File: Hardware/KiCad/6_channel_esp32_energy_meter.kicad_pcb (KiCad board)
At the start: 2 copper layers, 61 x 62.2 mm, 114 parts, among them IC1 ATM90E32AS, IC2 ATM90E32AS, IC3 LMR14020SDDA, J1 CONN_04, J16 PINHD-1X19, J2 CONN_04, J3 CONN_023.5MM, J4 9-12VAC, J5 PINHD1X1-SM1X01_SM, J6 PINHD1X1-SM1X01_SM, J8 PINHD1X1-SM1X01_SM, J9 PKS019-4011-0, U1 ESP32-DEVKITC-32D, Y1 16.384MHz, Y2 16.384MHz

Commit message: Make the schematic not terrible.
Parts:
- removed BR1: 50V/2A, 6_channel_esp32_energy_meter:SOP270P700X270-4
- removed C35: 10nF, 6_channel_esp32_energy_meter:C0603
- removed C36: 100uF/6.3V/1210, 6_channel_esp32_energy_meter:C1210
- removed CF1-2: BLU, 6_channel_esp32_energy_meter:CHIPLED_0603
- removed CT4-2, CT5-2, CT6-2: SJ2-35813B-SMT-TR, 6_channel_esp32_energy_meter:CUI_SJ2-35813B-SMT-TR
- removed D1: DIODE-DO214AC, 6_channel_esp32_energy_meter:DO214AC
- removed FD1, FD2: FIDUCIALUFIDUCIAL, 6_channel_esp32_energy_meter:FIDUCIAL-MICRO
- removed IC3: LMR14020SDDA, 6_channel_esp32_energy_meter:SOIC127P600X170-9N
- removed J16: PINHD-1X19, 6_channel_esp32_energy_meter:1X19
- removed J3: CONN_023.5MM, 6_channel_esp32_energy_meter:SCREWTERMINAL-3.5MM-2
- removed J4: 9-12VAC, 6_channel_esp32_energy_meter:CUI_PJ-002AH-SMT-TR
- removed J5, J6, J8: PINHD1X1-SM1X01_SM, 6_channel_esp32_energy_meter:1X01-SM
- removed J9: PKS019-4011-0, 6_channel_esp32_energy_meter:PKS01940110
- removed JP1, JP12, JP13, JP2, JP3, JP4, JP5, JP6: JUMPER-SMT_2_NC_TRACE_SILK, 6_channel_esp32_energy_meter:SMT-JUMPER_2_NC_TRACE_SILK
- removed L1: 3.3uH / 8x8mm, 6_channel_esp32_energy_meter:INDPM8082X300N
- removed LOGO1: OSHW-LOGOS, 6_channel_esp32_energy_meter:OSHW-LOGO-S
- removed PWR1: GRN, 6_channel_esp32_energy_meter:CHIPLED_0603
- removed U1: ESP32-DEVKITC-32D, 6_channel_esp32_energy_meter:MODULE_ESP32-DEVKITC-32D
- removed ZX0, ZX0-2, ZX1-2, ZX2-2: WIREPADSMD1,27-254, 6_channel_esp32_energy_meter:SMD1,27-2,54
- added CF2: BLU, 6_channel_esp32_energy_meter:CHIPLED_0603, F.Cu at (155.5, 113.0)
- added CF3: BLU, 6_channel_esp32_energy_meter:CHIPLED_0603, F.Cu at (153.8, 115.0)
- added CF4: BLU, 6_channel_esp32_energy_meter:CHIPLED_0603, F.Cu at (184.9, 83.3)
- added CF5: BLU, 6_channel_esp32_energy_meter:CHIPLED_0603, F.Cu at (186.6, 81.3)
- added CF6: BLU, 6_channel_esp32_energy_meter:CHIPLED_0603, F.Cu at (193.1, 75.2)
- added CF7: BLU, 6_channel_esp32_energy_meter:CHIPLED_0603, F.Cu at (122.6, 64.0)
- added CT1-1: SJ2-35813B-SMT-TR, 6_channel_esp32_energy_meter:CUI_SJ2-35813B-SMT-TR, F.Cu at (97.2, 74.9)
- added CT2-1: SJ2-35813B-SMT-TR, 6_channel_esp32_energy_meter:CUI_SJ2-35813B-SMT-TR, F.Cu at (97.2, 86.4)
- added CT3-1: SJ2-35813B-SMT-TR, 6_channel_esp32_energy_meter:CUI_SJ2-35813B-SMT-TR, F.Cu at (97.2, 97.8)
- added R25: 20K, Resistor_SMD:R_0603_1608Metric_Pad1.05x0.95mm_HandSolder, F.Cu at (168.9, 90.8)
- added R27: 20K, Resistor_SMD:R_0603_1608Metric_Pad1.05x0.95mm_HandSolder, F.Cu at (158.0, 86.5)
- added R29: 22, Resistor_SMD:R_0603_1608Metric_Pad1.05x0.95mm_HandSolder, F.Cu at (169.9, 87.0)
- added R30: 22, Resistor_SMD:R_0603_1608Metric_Pad1.05x0.95mm_HandSolder, F.Cu at (192.8, 73.1)
- added R31: 22, Resistor_SMD:R_0603_1608Metric_Pad1.05x0.95mm_HandSolder, F.Cu at (155.0, 88.5)
- added R33: 100, Resistor_SMD:R_0603_1608Metric_Pad1.05x0.95mm_HandSolder, F.Cu at (184.6, 81.1)
- added R35: 100, Resistor_SMD:R_0603_1608Metric_Pad1.05x0.95mm_HandSolder, F.Cu at (183.4, 71.1)
- added R36: 100, Resistor_SMD:R_0603_1608Metric_Pad1.05x0.95mm_HandSolder, F.Cu at (180.4, 73.1)
- added R37: 100, Resistor_SMD:R_0603_1608Metric_Pad1.05x0.95mm_HandSolder, F.Cu at (158.0, 88.5)
- added R38: 100, Resistor_SMD:R_0603_1608Metric_Pad1.05x0.95mm_HandSolder, F.Cu at (165.9, 85.0)
- added R39: 1K, Resistor_SMD:R_0603_1608Metric_Pad1.05x0.95mm_HandSolder, F.Cu at (175.7, 82.4)
- added R40: 1K, Resistor_SMD:R_0603_1608Metric_Pad1.05x0.95mm_HandSolder, F.Cu at (186.9, 79.1)
- added R41: 10K, Resistor_SMD:R_0603_1608Metric_Pad1.05x0.95mm_HandSolder, F.Cu at (180.4, 71.1)
- added R42: 220, Resistor_SMD:R_0603_1608Metric_Pad1.05x0.95mm_HandSolder, F.Cu at (172.9, 87.0)
- added R43: 10K, Resistor_SMD:R_0603_1608Metric_Pad1.05x0.95mm_HandSolder, F.Cu at (163.9, 87.0)
- added R44: 1k, Resistor_SMD:R_0603_1608Metric_Pad1.05x0.95mm_HandSolder, F.Cu at (168.9, 85.0)
- added R45: 1k, Resistor_SMD:R_0603_1608Metric_Pad1.05x0.95mm_HandSolder, F.Cu at (183.9, 75.1)
- added R46: 1k, Resistor_SMD:R_0603_1608Metric_Pad1.05x0.95mm_HandSolder, F.Cu at (183.9, 73.1)
- added R47: 1k, 6_channel_esp32_energy_meter:R0603, F.Cu at (131.6, 69.1)
- added ZX10: WIREPADSMD1,27-254, 6_channel_esp32_energy_meter:SMD1,27-2,54, F.Cu at (189.0, 77.4)
- added ZX11: WIREPADSMD1,27-254, 6_channel_esp32_energy_meter:SMD1,27-2,54, F.Cu at (192.0, 75.4)
- added ZX12: WIREPADSMD1,27-254, 6_channel_esp32_energy_meter:SMD1,27-2,54, F.Cu at (183.8, 83.4)
- added ZX13: WIREPADSMD1,27-254, 6_channel_esp32_energy_meter:SMD1,27-2,54, F.Cu at (181.0, 86.7)
- added ZX14: WIREPADSMD1,27-254, 6_channel_esp32_energy_meter:SMD1,27-2,54, F.Cu at (190.3, 77.4)
- added ZX3: WIREPADSMD1,27-254, 6_channel_esp32_energy_meter:SMD1,27-2,54, F.Cu at (149.9, 118.4)
- added ZX4: WIREPADSMD1,27-254, 6_channel_esp32_energy_meter:SMD1,27-2,54, F.Cu at (137.6, 108.3)
- added ZX5: WIREPADSMD1,27-254, 6_channel_esp32_energy_meter:SMD1,27-2,54, F.Cu at (143.3, 95.1)
- added ZX6: WIREPADSMD1,27-254, 6_channel_esp32_energy_meter:SMD1,27-2,54, F.Cu at (136.3, 108.3)
- added ZX7: WIREPADSMD1,27-254, 6_channel_esp32_energy_meter:SMD1,27-2,54, F.Cu at (143.3, 97.6)
- added ZX8: WIREPADSMD1,27-254, 6_channel_esp32_energy_meter:SMD1,27-2,54, F.Cu at (195.9, 64.1)
- added ZX9: WIREPADSMD1,27-254, 6_channel_esp32_energy_meter:SMD1,27-2,54, F.Cu at (195.9, 66.7)
- C1, C10, C26, C9: value 0.1uF -> 18nF
- C14, C29: value 18nF -> 10uF
- C15, C30: value 18nF -> 0.1uF
- C17: value .33uF -> 0.1uF
- C18, C22, C5: value .33uF -> 18nF
- C23, C8: value 10uF -> .33uF
- C24, C25: value 0.1uF -> .33uF
- C27: value 10uF -> 18nF
- C31: value 0.1uF -> 10uF
- C32: value 220pF -> 0.1uF
- C33: value 100uF/25V -> 0.1uF; footprint 6_channel_esp32_energy_meter:UD-6,3X7,7_NICHICON -> 6_channel_esp32_energy_meter:C0603
- C34: value 10uF/25V -> 0.1uF; footprint 6_channel_esp32_energy_meter:C0805 -> 6_channel_esp32_energy_meter:C0603
- IC1, IC2: value ATM90E32AS -> ATM90E36
- J1: value CONN_04 -> Conn_02x05_Odd_Even; footprint 6_channel_esp32_energy_meter:1X04 -> Connector_IDC:IDC-Header_2x05_P2.54mm_Vertical
- J2: value CONN_04 -> Conn_02x07_Odd_Even; footprint 6_channel_esp32_energy_meter:1X04 -> Connector_IDC:IDC-Header_2x07_P2.54mm_Vertical
- R1: value 10K -> 20K; footprint 6_channel_esp32_energy_meter:R0603 -> Resistor_SMD:R_0603_1608Metric_Pad1.05x0.95mm_HandSolder
- R10: value 1k -> 100; footprint 6_channel_esp32_energy_meter:R0603 -> Resistor_SMD:R_0603_1608Metric_Pad1.05x0.95mm_HandSolder
- R11: value 1K -> 100; footprint 6_channel_esp32_energy_meter:RA1206-8 -> Resistor_SMD:R_0603_1608Metric_Pad1.05x0.95mm_HandSolder
- R12: value 10K -> 100; footprint 6_channel_esp32_energy_meter:R0603 -> Resistor_SMD:R_0603_1608Metric_Pad1.05x0.95mm_HandSolder
- R13: value 10K -> 100; footprint 6_channel_esp32_energy_meter:RA1206-8 -> Resistor_SMD:R_0603_1608Metric_Pad1.05x0.95mm_HandSolder
- R14, R24: footprint 6_channel_esp32_energy_meter:RA1206-8 -> Resistor_SMD:R_0603_1608Metric_Pad1.05x0.95mm_HandSolder
- R15, R6, R7, R8: footprint 6_channel_esp32_energy_meter:R0603 -> Resistor_SMD:R_0603_1608Metric_Pad1.05x0.95mm_HandSolder
- R16, R5: value 100 -> 1K; footprint 6_channel_esp32_energy_meter:R0603 -> Resistor_SMD:R_0603_1608Metric_Pad1.05x0.95mm_HandSolder
- R17: value 22 -> 1K; footprint 6_channel_esp32_energy_meter:R0603 -> Resistor_SMD:R_0603_1608Metric_Pad1.05x0.95mm_HandSolder
- R18: value 22 -> 10K; footprint 6_channel_esp32_energy_meter:R0603 -> Resistor_SMD:R_0603_1608Metric_Pad1.05x0.95mm_HandSolder
- R19: value 22 -> 220; footprint 6_channel_esp32_energy_meter:R0603 -> Resistor_SMD:R_0603_1608Metric_Pad1.05x0.95mm_HandSolder
- R2: value 10K -> 20K; footprint 6_channel_esp32_energy_meter:RA1206-8 -> Resistor_SMD:R_0603_1608Metric_Pad1.05x0.95mm_HandSolder
- R20: value 1k -> 10K; footprint 6_channel_esp32_energy_meter:R0603 -> Resistor_SMD:R_0603_1608Metric_Pad1.05x0.95mm_HandSolder
- R21: value 20k -> 1k; footprint 6_channel_esp32_energy_meter:R0603 -> Resistor_SMD:R_0603_1608Metric_Pad1.05x0.95mm_HandSolder
- R22: value 34k -> 1k; footprint 6_channel_esp32_energy_meter:R0603 -> Resistor_SMD:R_0603_1608Metric_Pad1.05x0.95mm_HandSolder
- R23: value 10k -> 1k; footprint 6_channel_esp32_energy_meter:R0603 -> Resistor_SMD:R_0603_1608Metric_Pad1.05x0.95mm_HandSolder
- R26: value 20k 1/4W -> 20K; footprint 6_channel_esp32_energy_meter:R0603 -> Resistor_SMD:R_0603_1608Metric_Pad1.05x0.95mm_HandSolder
- R28, R32: value 20k 1/4W -> 1K; footprint 6_channel_esp32_energy_meter:R0603 -> Resistor_SMD:R_0603_1608Metric_Pad1.05x0.95mm_HandSolder
- R3: value 100 -> 20K; footprint 6_channel_esp32_energy_meter:RA1206-8 -> Resistor_SMD:R_0603_1608Metric_Pad1.05x0.95mm_HandSolder
- R34: value 20k 1/4W -> 100; footprint 6_channel_esp32_energy_meter:R0603 -> Resistor_SMD:R_0603_1608Metric_Pad1.05x0.95mm_HandSolder
- R4: value 100 -> 20K; footprint 6_channel_esp32_energy_meter:R0603 -> Resistor_SMD:R_0603_1608Metric_Pad1.05x0.95mm_HandSolder
- R9: value 1k -> 1K; footprint 6_channel_esp32_energy_meter:R0603 -> Resistor_SMD:R_0603_1608Metric_Pad1.05x0.95mm_HandSolder
- ZX1, ZX2: moved to F.Cu
- moved CT4 100.1 mm to (107.3, 39.4), turned to 270 degrees
- moved CT5 82.9 mm to (107.3, 50.8), turned to 270 degrees
- moved CT6 70.8 mm to (107.3, 62.2), turned to 270 degrees
- moved J1 68.1 mm to (188.6, 102.2), turned to 0 degrees
- moved C34 62.6 mm to (180.8, 84.4), turned to 0 degrees
- moved C31 61.7 mm to (186.9, 77.1), turned to 0 degrees
- moved C32 57.9 mm to (189.9, 75.1), turned to 0 degrees
- moved C26 55.9 mm to (192.4, 71.1), turned to 0 degrees
- moved CT3-2 55.7 mm to (97.2, 63.5)
- moved CT2-2 53.5 mm to (97.2, 52.1)
- moved CT1-2 51.3 mm to (97.2, 40.6)
- moved C23 50.3 mm to (186.9, 75.1), turned to 0 degrees
- moved C33 48.7 mm to (178.9, 86.4), turned to 0 degrees
- moved R32 48.4 mm to (189.4, 71.1), turned to 0 degrees
- moved R10 48.0 mm to (131.2, 108.0), turned to 0 degrees
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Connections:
- C1 pad 1: GND -> (no net)
- C1 pad 2: Net-(C1-Pad2) -> (no net)
- C10 pad 1: GND -> (no net)
- C10 pad 2: VDD -> (no net)
- C11 pad 1: GND -> (no net)
- C11 pad 2: VDD -> (no net)
- C12 pad 1: Net-(C12-Pad1) -> (no net)
- C12 pad 2: GND -> (no net)
- C13 pad 1: Net-(C12-Pad1) -> (no net)
- C13 pad 2: GND -> (no net)
- C14 pad 1: VAP -> (no net)
- C14 pad 2: GND -> (no net)
- C15 pad 1: VAN -> (no net)
- C15 pad 2: GND -> (no net)
- C16 pad 1: GND -> (no net)
- C16 pad 2: Net-(C16-Pad2) -> (no net)
- C17 pad 1: /6_channel_esp32_energy_meter_2/IAP-2 -> (no net)
- C17 pad 2: GND -> (no net)
- C18 pad 1: GND -> (no net)
- C18 pad 2: /6_channel_esp32_energy_meter_2/IAN-2 -> (no net)
- C19 pad 1: /6_channel_esp32_energy_meter_2/IBP-2 -> (no net)
- C19 pad 2: GND -> (no net)
- C2 pad 1: /6_channel_esp32_energy_meter_1/IAP -> (no net)
- C2 pad 2: GND -> (no net)
- C20 pad 1: GND -> (no net)
- C20 pad 2: /6_channel_esp32_energy_meter_2/IBN-2 -> (no net)
- C21 pad 1: /6_channel_esp32_energy_meter_2/ICP-2 -> (no net)
- C21 pad 2: GND -> (no net)
- C22 pad 1: GND -> (no net)
- C22 pad 2: /6_channel_esp32_energy_meter_2/ICN-2 -> (no net)
- C23 pad 1: GND -> (no net)
- C23 pad 2: Net-(C23-Pad2) -> (no net)
- C24 pad 1: GND -> (no net)
- C24 pad 2: Net-(C23-Pad2) -> (no net)
- C25 pad 1: GND -> (no net)
- C25 pad 2: VDD -> (no net)
- C26 pad 1: GND -> (no net)
- C26 pad 2: VDD -> (no net)
- C27 pad 1: Net-(C27-Pad1) -> (no net)
- C27 pad 2: GND -> (no net)
- C28 pad 1: Net-(C27-Pad1) -> (no net)
- C28 pad 2: GND -> (no net)
- C29 pad 1: VAP2 -> (no net)
- C29 pad 2: GND -> (no net)
- C3 pad 1: GND -> (no net)
- C3 pad 2: /6_channel_esp32_energy_meter_1/IAN -> (no net)
- C30 pad 1: VAN2 -> (no net)
- C30 pad 2: GND -> (no net)
- C31 pad 1: Net-(C31-Pad1) -> (no net)
- C31 pad 2: Net-(C31-Pad2) -> (no net)
- C32 pad 1: VDD -> (no net)
- C32 pad 2: Net-(C32-Pad2) -> (no net)
- C34 pad 1: Net-(BR1-Pad1) -> (no net)
- C34 pad 2: GND -> (no net)
- C4 pad 1: /6_channel_esp32_energy_meter_1/IBP -> (no net)
- C4 pad 2: GND -> (no net)
- C5 pad 1: GND -> (no net)
- C5 pad 2: /6_channel_esp32_energy_meter_1/IBN -> (no net)
- C6 pad 1: /6_channel_esp32_energy_meter_1/ICP -> (no net)
- C6 pad 2: GND -> (no net)
- C7 pad 1: GND -> (no net)
- C7 pad 2: /6_channel_esp32_energy_meter_1/ICN -> (no net)
- C8 pad 1: GND -> (no net)
- C8 pad 2: Net-(C8-Pad2) -> (no net)
- C9 pad 1: GND -> (no net)
- C9 pad 2: Net-(C8-Pad2) -> (no net)
- CT1 pad 1: IA- -> Net-(CT1-1-Pad1)
- CT1 pad 2: IA+ -> Net-(CT1-1-Pad2)
- CT1-2 pad 1: IA- -> Net-(CT1-2-Pad1)
- CT1-2 pad 2: IA+ -> Net-(CT1-2-Pad2)
- CT2 pad 1: IB- -> Net-(CT2-1-Pad1)
- CT2 pad 2: IB+ -> Net-(CT2-1-Pad2)
- CT2-2 pad 1: IB- -> Net-(CT2-2-Pad1)
- CT2-2 pad 2: IB+ -> Net-(CT2-2-Pad2)
- CT3 pad 1: IC- -> Net-(CT3-1-Pad1)
- CT3 pad 2: IC+ -> Net-(CT3-1-Pad2)
- CT3-2 pad 1: IC- -> Net-(CT3-2-Pad1)
- CT3-2 pad 2: IC+ -> Net-(CT3-2-Pad2)
- CT4 pad 1: IA--2 -> Net-(CT1-2-Pad1)
- CT4 pad 2: IA+-2 -> Net-(CT1-2-Pad2)
- CT5 pad 1: IB--2 -> Net-(CT2-2-Pad1)
- CT5 pad 2: IB+-2 -> Net-(CT2-2-Pad2)
- CT6 pad 1: IC--2 -> Net-(CT3-2-Pad1)
- CT6 pad 2: IC+-2 -> Net-(CT3-2-Pad2)
- IC1 pad 1: VDD -> +3V3
- IC1 pad 10: Net-(IC1-Pad10) -> GND
- IC1 pad 11: Net-(C12-Pad1) -> Net-(IC1-Pad11)
- IC1 pad 13: VAP -> Net-(IC1-Pad13)
- IC1 pad 14: VAN -> Net-(IC1-Pad14)
- IC1 pad 15: VAP -> Net-(IC1-Pad15)
- IC1 pad 16: VAN -> Net-(IC1-Pad16)
- IC1 pad 17: VAP -> Net-(IC1-Pad17)
- IC1 pad 18: VAN -> Net-(IC1-Pad18)
- IC1 pad 22: /6_channel_esp32_energy_meter_1/ZX0 -> Net-(IC1-Pad22)
- IC1 pad 23: /6_channel_esp32_energy_meter_1/ZX1 -> Net-(IC1-Pad23)
- IC1 pad 24: /6_channel_esp32_energy_meter_1/ZX2 -> Net-(IC1-Pad24)
- IC1 pad 25: /6_channel_esp32_energy_meter_1/CF1 -> Net-(IC1-Pad25)
- IC1 pad 26: /6_channel_esp32_energy_meter_1/CF2 -> Net-(IC1-Pad26)
- IC1 pad 27: /6_channel_esp32_energy_meter_1/CF3 -> Net-(IC1-Pad27)
- IC1 pad 28: /6_channel_esp32_energy_meter_1/CF4 -> Net-(IC1-Pad28)
- IC1 pad 29: WARN -> Net-(IC1-Pad29)
- IC1 pad 3: /6_channel_esp32_energy_meter_1/IAP -> Net-(IC1-Pad3)
- IC1 pad 30: IRQ0 -> Net-(IC1-Pad30)
- IC1 pad 31: IRQ1 -> /meter_1/IRQ1
- IC1 pad 33: VDD -> +3V3
- IC1 pad 34: VDD -> +3V3
- IC1 pad 37: ~CS -> /meter_1/~CS
- IC1 pad 38: SCLK -> /meter_1/SCLK
- IC1 pad 39: MISO -> Net-(IC1-Pad39)
- IC1 pad 4: /6_channel_esp32_energy_meter_1/IAN -> Net-(IC1-Pad4)
- IC1 pad 40: MOSI -> /meter_1/SDI
- IC1 pad 41: Net-(C1-Pad2) -> /meter_1/~RESET
- IC1 pad 42: Net-(C8-Pad2) -> +3V3
- IC1 pad 43: Net-(C8-Pad2) -> +3V3
- IC1 pad 48: VDD -> +3V3
- IC1 pad 5: /6_channel_esp32_energy_meter_1/IBP -> Net-(IC1-Pad5)
- IC1 pad 6: /6_channel_esp32_energy_meter_1/IBN -> Net-(IC1-Pad6)
- IC1 pad 7: /6_channel_esp32_energy_meter_1/ICP -> Net-(IC1-Pad7)
- IC1 pad 8: /6_channel_esp32_energy_meter_1/ICN -> Net-(IC1-Pad8)
- IC1 pad 9: Net-(IC1-Pad9) -> GND
- IC2 pad 1: VDD -> +3V3
- IC2 pad 10: Net-(IC2-Pad10) -> GND
- IC2 pad 11: Net-(C27-Pad1) -> Net-(IC2-Pad11)
- IC2 pad 13: VAP2 -> Net-(IC2-Pad13)
- IC2 pad 14: VAN2 -> Net-(IC2-Pad14)
- IC2 pad 15: VAP2 -> Net-(IC2-Pad15)
- IC2 pad 16: VAN2 -> Net-(IC2-Pad16)
- IC2 pad 17: VAP2 -> Net-(IC2-Pad17)
- IC2 pad 18: VAN2 -> Net-(IC2-Pad18)
- IC2 pad 22: /6_channel_esp32_energy_meter_2/ZX0-2 -> Net-(IC2-Pad22)
- IC2 pad 23: /6_channel_esp32_energy_meter_2/ZX1-2 -> Net-(IC2-Pad23)
- IC2 pad 24: /6_channel_esp32_energy_meter_2/ZX2-2 -> Net-(IC2-Pad24)
- IC2 pad 25: /6_channel_esp32_energy_meter_2/CF1-2 -> Net-(IC2-Pad25)
- IC2 pad 26: /6_channel_esp32_energy_meter_2/CF2-2 -> Net-(IC2-Pad26)
- IC2 pad 27: /6_channel_esp32_energy_meter_2/CF3-2 -> Net-(IC2-Pad27)
- IC2 pad 28: /6_channel_esp32_energy_meter_2/CF4-2 -> Net-(IC2-Pad28)
- IC2 pad 29: WARN -> Net-(IC2-Pad29)
- IC2 pad 3: /6_channel_esp32_energy_meter_2/IAP-2 -> Net-(IC2-Pad3)
- IC2 pad 30: IRQ0 -> Net-(IC2-Pad30)
- IC2 pad 31: IRQ1 -> /meter_2/IRQ1
- IC2 pad 33: VDD -> +3V3
- IC2 pad 34: VDD -> +3V3
- IC2 pad 37: ~CS-2 -> /meter_2/~CS
- IC2 pad 38: SCLK -> /meter_1/SCLK
- IC2 pad 39: MISO -> Net-(IC2-Pad39)
- IC2 pad 4: /6_channel_esp32_energy_meter_2/IAN-2 -> Net-(IC2-Pad4)
- IC2 pad 40: MOSI -> /meter_1/SDI
- IC2 pad 41: Net-(C16-Pad2) -> /meter_1/~RESET
- IC2 pad 42: Net-(C23-Pad2) -> +3V3
- IC2 pad 43: Net-(C23-Pad2) -> +3V3
- IC2 pad 48: VDD -> +3V3
- IC2 pad 5: /6_channel_esp32_energy_meter_2/IBP-2 -> Net-(IC2-Pad5)
- IC2 pad 6: /6_channel_esp32_energy_meter_2/IBN-2 -> Net-(IC2-Pad6)
- IC2 pad 7: /6_channel_esp32_energy_meter_2/ICP-2 -> Net-(IC2-Pad7)
- IC2 pad 8: /6_channel_esp32_energy_meter_2/ICN-2 -> Net-(IC2-Pad8)
- IC2 pad 9: Net-(IC2-Pad9) -> GND
- J1 pad 1: /6_channel_esp32_energy_meter_1/CF4 -> /meter_1/V1P
- J1 pad 2: /6_channel_esp32_energy_meter_1/CF3 -> /meter_1/V1N
- J1 pad 3: /6_channel_esp32_energy_meter_1/CF2 -> /meter_1/V1P
- J1 pad 4: /6_channel_esp32_energy_meter_1/CF1 -> /meter_1/V1N
- J2 pad 1: /6_channel_esp32_energy_meter_2/CF4-2 -> +3V3
- J2 pad 2: /6_channel_esp32_energy_meter_2/CF3-2 -> +3V3
- J2 pad 3: /6_channel_esp32_energy_meter_2/CF2-2 -> /meter_1/~CS
- J2 pad 4: /6_channel_esp32_energy_meter_2/CF1-2 -> /meter_2/~CS
- R1 pad 1: VDD -> (no net)
- R1 pad 2: Net-(C1-Pad2) -> (no net)
- R10 pad 1: Net-(PWR1-PadA) -> (no net)
- R10 pad 2: VDD -> (no net)
- R11 pad 1: GND -> (no net)
- R11 pad 2: GND -> (no net)
- R12 pad 1: VDD -> (no net)
- R12 pad 2: Net-(C16-Pad2) -> (no net)
- R13 pad 1: MOSI -> (no net)
- R13 pad 2: MISO -> (no net)
- R14 pad 1: IA+-2 -> (no net)
- R14 pad 2: IA--2 -> (no net)
- R15 pad 1: /6_channel_esp32_energy_meter_2/ICP-2 -> (no net)
- R15 pad 2: IC+-2 -> (no net)
- R16 pad 1: /6_channel_esp32_energy_meter_2/ICN-2 -> (no net)
- R16 pad 2: IC--2 -> (no net)
- R17 pad 1: Net-(JP6-Pad1) -> (no net)
- R17 pad 2: IC+-2 -> (no net)
- R18 pad 1: Net-(JP4-Pad1) -> (no net)
- R18 pad 2: IA+-2 -> (no net)
- R19 pad 1: Net-(JP5-Pad1) -> (no net)
- R19 pad 2: IB+-2 -> (no net)
- R2 pad 1: MOSI -> (no net)
- R2 pad 2: MISO -> (no net)
- R20 pad 1: Net-(CF1-2-PadA) -> (no net)
- R20 pad 2: /6_channel_esp32_energy_meter_2/CF1-2 -> (no net)
- R21 pad 1: GND -> (no net)
- R21 pad 2: Net-(IC3-Pad4) -> (no net)
- R22 pad 1: Net-(C32-Pad2) -> (no net)
- R22 pad 2: VDD -> (no net)
- R23 pad 1: GND -> (no net)
- R23 pad 2: Net-(C32-Pad2) -> (no net)
- R24 pad 1: VDD -> (no net)
- R24 pad 2: VDD -> (no net)
- R26 pad 1: VAP -> (no net)
- R26 pad 2: /6_channel_esp32_energy_meter_3/VA+ -> (no net)
- R28 pad 1: VAP2 -> (no net)
- R28 pad 2: /6_channel_esp32_energy_meter_3/VA2+ -> (no net)
- R3 pad 1: IA+ -> (no net)
- R3 pad 2: IA- -> (no net)
- R32 pad 1: VAN2 -> (no net)
- R32 pad 2: /6_channel_esp32_energy_meter_3/VA2- -> (no net)
- R34 pad 1: VAN -> (no net)
- R34 pad 2: /6_channel_esp32_energy_meter_3/VA- -> (no net)
- R4 pad 1: /6_channel_esp32_energy_meter_1/ICP -> (no net)
- R4 pad 2: IC+ -> (no net)
- R5 pad 1: /6_channel_esp32_energy_meter_1/ICN -> (no net)
- R5 pad 2: IC- -> (no net)
- R6 pad 1: Net-(JP3-Pad1) -> (no net)
- R6 pad 2: IC+ -> (no net)
- R7 pad 1: Net-(JP1-Pad1) -> (no net)
- R7 pad 2: IA+ -> (no net)
- R8 pad 1: Net-(JP2-Pad1) -> (no net)
- R8 pad 2: IB+ -> (no net)
- R9 pad 1: Net-(CF1-PadA) -> (no net)
- R9 pad 2: /6_channel_esp32_energy_meter_1/CF1 -> (no net)
- ZX1 pad 1: /6_channel_esp32_energy_meter_1/ZX1 -> Net-(IC1-Pad22)
- ZX2 pad 1: /6_channel_esp32_energy_meter_1/ZX2 -> Net-(IC1-Pad23)
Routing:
- net VDD: track 276.3 -> 0.00 mm, vias 10 -> 0
- net IC+: track 137.4 -> 0.00 mm, vias 3 -> 0
- net IC-: track 113.8 -> 0.00 mm, vias 1 -> 0
- net IB+: track 99.1 -> 0.00 mm, vias 3 -> 0
- net IB-: track 93.9 -> 0.00 mm, vias 2 -> 0
- net /6_channel_esp32_energy_meter_3/VA+: track 87.3 -> 0.00 mm, vias 2 -> 0
- net IRQ0: track 81.0 -> 0.00 mm, vias 3 -> 0
- net IRQ1: track 76.1 -> 0.00 mm, vias 3 -> 0
- net /6_channel_esp32_energy_meter_1/CF1: track 75.2 -> 0.00 mm, vias 3 -> 0
- net IA--2: track 72.5 -> 0.00 mm, vias 1 -> 0
- net /6_channel_esp32_energy_meter_1/CF4: track 72.0 -> 0.00 mm, vias 3 -> 0
- net IA+: track 71.8 -> 0.00 mm, vias 3 -> 0
- net MOSI: track 70.9 -> 0.00 mm, vias 4 -> 0
- net /6_channel_esp32_energy_meter_1/CF3: track 70.0 -> 0.00 mm, vias 3 -> 0
- net /6_channel_esp32_energy_meter_3/VA-: track 69.5 -> 0.00 mm, vias 6 -> 0
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- removed copper zone on B.Cu, net GND
- removed copper zone on F.Cu, net GND
- removed copper zone on F.Cu, net Net-(BR1-Pad1)
- removed copper zone on F.Cu, net Net-(C31-Pad2)
- removed copper zone on F.Cu, net VDD
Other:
- board outline removed
- net class Default: clearance 0.1524 -> 0.2
- rule pad_to_mask_clearance: 0.2 -> 0
- rule trace_clearance: 0.1524 -> 0.2
- board text removed: "+"
- board text removed: "0"
- board text removed: "12"
- board text removed: "13"
- board text removed: "14"
- board text removed: "15"
- board text removed: "16"
- board text removed: "17"
- board text removed: "2"
- board text removed: "21"
- board text removed: "22"
- board text removed: "25"
- board text removed: "26"
- board text removed: "27"
- board text removed: "35"
- board text removed: "3V3"
- board text removed: "3V3 OUT"
- board text removed: "9-12 VAC Only"
- board text removed: "CF1"
- board text removed: "CF1-2"
- board text removed: "CF2"
- board text removed: "CF2-2"
- board text removed: "CF3"
- board text removed: "CF3-2"
- board text removed: "CF4"
- board text removed: "CF4-2"
- board text removed: "CLK"
- board text removed: "CS"
- board text removed: "CS2"
- board text removed: "CircuitSetup.us ESP32 Energy Meter v1.4 rev1"
- board text removed: "Energy Pulse"
- board text removed: "For JP1-JP6, if your CT sensors have a burden resistor built in, sever corresponding traces to disable 22ohm burden resistor for CT1-CT6"
- board text removed: "GND"
- board text removed: "IRQ0"
- board text removed: "IRQ1"
- board text removed: "MISO"
- board text removed: "MOSI"
- board text removed: "NOTE: A 9 to 12V AC transformer is required to measure voltage and power this board. Do NOT input more than 12VAC For detailed documentation, please visit CircuitSetup.us"
- board text removed: "Pulse outputs: CF1: Active energy CF2: Reactive/apparent energy CF3: Active fundamental energy CF4: Active harmonic energy"
- board text removed: "SCLK"
- board text removed: "Sever JP12 & JP13 to use VA2+ as secondary voltage measurement input. VA2+ should be hooked up to a second AC transformer on a different phase than the primary transformer. DO NOT connect both without severing these connections first!"
- board text removed: "VA+"
- board text removed: "VA-"
- board text removed: "VA2+"
- board text removed: "VA2-"
- board text removed: "WARN"
- board text removed: "ZX2/ZX1/ZX0: Zero-Crossing Outputs"

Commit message: Working on layout.
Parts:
- removed R47: 1k, 6_channel_esp32_energy_meter:R0603
- removed ZX1, ZX10, ZX11, ZX12, ZX13, ZX14, ZX2, ZX3, ZX4, ZX5, ZX6, ZX7, ZX8, ZX9: WIREPADSMD1,27-254, 6_channel_esp32_energy_meter:SMD1,27-2,54
- added C35: 0.1uF, Capacitor_SMD:C_0603_1608Metric_Pad1.05x0.95mm_HandSolder, F.Cu at (74.0, 95.0)
- added C36: 10uF, Capacitor_SMD:C_1206_3216Metric_Pad1.42x1.75mm_HandSolder, F.Cu at (76.0, 94.2)
- added C37: 10uF, Capacitor_SMD:C_1206_3216Metric_Pad1.42x1.75mm_HandSolder, F.Cu at (72.0, 57.2)
- added C38: 0.1uF, Capacitor_SMD:C_0603_1608Metric_Pad1.05x0.95mm_HandSolder, F.Cu at (70.0, 58.0)
- added C39: 0.1uF, Capacitor_SMD:C_0603_1608Metric_Pad1.05x0.95mm_HandSolder, F.Cu at (70.0, 95.0)
- added H1: MountingHole, MountingHole:MountingHole_3.2mm_M3_Pad_Via, F.Cu at (40.0, 130.0)
- added H2: MountingHole, MountingHole:MountingHole_3.2mm_M3_Pad_Via, F.Cu at (90.0, 65.0)
- added H3: MountingHole, MountingHole:MountingHole_3.2mm_M3_Pad_Via, F.Cu at (40.0, 40.0)
- added H4: MountingHole, MountingHole:MountingHole_3.2mm_M3_Pad_Via, F.Cu at (90.0, 130.0)
- added H5: MountingHole, MountingHole:MountingHole_3.2mm_M3_Pad_Via, F.Cu at (90.0, 40.0)
- C1: value 18nF -> 0.1uF; footprint 6_channel_esp32_energy_meter:C0603 -> Capacitor_SMD:C_0603_1608Metric_Pad1.05x0.95mm_HandSolder
- C10, C27, C5, C9: value 18nF -> 0.33uF; footprint 6_channel_esp32_energy_meter:C0603 -> Capacitor_SMD:C_0603_1608Metric_Pad1.05x0.95mm_HandSolder
- C11, C28: value 0.1uF -> 0.33uF; footprint 6_channel_esp32_energy_meter:C0603 -> Capacitor_SMD:C_0603_1608Metric_Pad1.05x0.95mm_HandSolder
- C12, C31: value 10uF -> 18nF; footprint 6_channel_esp32_energy_meter:C0603 -> Capacitor_SMD:C_0603_1608Metric_Pad1.05x0.95mm_HandSolder
- C13, C30: value 0.1uF -> 18nF; footprint 6_channel_esp32_energy_meter:C0603 -> Capacitor_SMD:C_0603_1608Metric_Pad1.05x0.95mm_HandSolder
- C14: value 10uF -> 0.1uF; footprint 6_channel_esp32_energy_meter:C0603 -> Capacitor_SMD:C_0603_1608Metric_Pad1.05x0.95mm_HandSolder
- C15, C33: value 0.1uF -> 10uF; footprint 6_channel_esp32_energy_meter:C0603 -> Capacitor_SMD:C_1206_3216Metric_Pad1.42x1.75mm_HandSolder
- C16, C17, C22, C26, C32, C34: footprint 6_channel_esp32_energy_meter:C0603 -> Capacitor_SMD:C_0603_1608Metric_Pad1.05x0.95mm_HandSolder
- C18: value 18nF -> 10uF; footprint 6_channel_esp32_energy_meter:C0603 -> Capacitor_SMD:C_1206_3216Metric_Pad1.42x1.75mm_HandSolder
- C19: value .33uF -> 10uF; footprint 6_channel_esp32_energy_meter:C0603 -> Capacitor_SMD:C_1206_3216Metric_Pad1.42x1.75mm_HandSolder
- C2, C3: value .33uF -> CP1; footprint 6_channel_esp32_energy_meter:C0603 -> Capacitor_THT:CP_Radial_D12.5mm_P5.00mm
- C20, C21: value .33uF -> 0.1uF; footprint 6_channel_esp32_energy_meter:C0603 -> Capacitor_SMD:C_0603_1608Metric_Pad1.05x0.95mm_HandSolder
- C23, C24, C25, C6, C7: value .33uF -> 0.33uF; footprint 6_channel_esp32_energy_meter:C0603 -> Capacitor_SMD:C_0603_1608Metric_Pad1.05x0.95mm_HandSolder
- C29: value 10uF -> 0.33uF; footprint 6_channel_esp32_energy_meter:C0603 -> Capacitor_SMD:C_0603_1608Metric_Pad1.05x0.95mm_HandSolder
- C4, C8: value .33uF -> 18nF; footprint 6_channel_esp32_energy_meter:C0603 -> Capacitor_SMD:C_0603_1608Metric_Pad1.05x0.95mm_HandSolder
- R1: value 20K -> 10K
- R10, R11, R33: value 100 -> 22R
- R12, R13, R14, R15, R34, R35, R36, R37, R38: value 100 -> 100R
- R16, R17, R39: value 1K -> 100R
- R18, R41: value 10K -> 1K
- R19: value 220 -> 1K
- R2: value 20K -> 1k
- R20: value 10K -> 100R
- R21: value 1k -> 10K
- R22, R23, R44, R45, R46: value 1k -> 1K
- R24: value 20K -> 1K
- R28, R5: value 1K -> 20K
- R29, R30, R7, R8: value 22 -> 1K
- R31: value 22 -> 22R
- R32, R9: value 1K -> 22R
- R42: value 220 -> 100R
- R6: value 22 -> 20K
- moved R32 133.7 mm to (59.5, 103.0), turned to 90 degrees
- moved C29 131.0 mm to (62.0, 112.8), turned to 180 degrees
- moved R33 129.6 mm to (59.5, 115.0), turned to 90 degrees
- moved C26 128.1 mm to (71.2, 112.8)
- moved C32 127.9 mm to (66.0, 107.0), turned to 180 degrees
- moved R30 127.4 mm to (71.2, 111.2), turned to 180 degrees
- moved C23 126.2 mm to (62.0, 93.2), turned to 180 degrees
- moved C20 125.7 mm to (66.8, 98.4), turned to 90 degrees
- moved C19 125.5 mm to (72.0, 94.2), turned to 90 degrees
- moved R35 123.2 mm to (62.0, 91.8)
- moved J1 123.0 mm to (68.2, 127.5), turned to 90 degrees
- moved R36 122.0 mm to (62.0, 102.2)
- moved C22 121.2 mm to (68.0, 112.8), turned to 180 degrees
- moved C25 120.4 mm to (62.0, 117.2), turned to 180 degrees
- moved R39 118.5 mm to (62.0, 115.8)
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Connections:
- C1 pad 1: (no net) -> /meter_1/~RESET
- C1 pad 2: (no net) -> GND
- C10 pad 1: (no net) -> /meter_1/I2P
- C10 pad 2: (no net) -> GND
- C11 pad 1: (no net) -> /meter_1/I3P
- C11 pad 2: (no net) -> GND
- C12 pad 1: (no net) -> Net-(C12-Pad1)
- C12 pad 2: (no net) -> GND
- C13 pad 1: (no net) -> Net-(C13-Pad1)
- C13 pad 2: (no net) -> GND
- C14 pad 1: (no net) -> Net-(C14-Pad1)
- C14 pad 2: (no net) -> GND
- C15 pad 1: (no net) -> Net-(C14-Pad1)
- C15 pad 2: (no net) -> GND
- C16 pad 1: (no net) -> +3V3
- C16 pad 2: (no net) -> GND
- C17 pad 1: (no net) -> /meter_1/1.8VDD
- C17 pad 2: (no net) -> GND
- C18 pad 1: (no net) -> /meter_1/1.8VDD
- C18 pad 2: (no net) -> GND
- C19 pad 1: (no net) -> +3V3
- C19 pad 2: (no net) -> GND
- C2 pad 1: (no net) -> +3V3
- C2 pad 2: (no net) -> GND
- C20 pad 1: (no net) -> +3V3
- C20 pad 2: (no net) -> GND
- C21 pad 1: (no net) -> +3V3
- C21 pad 2: (no net) -> GND
- C22 pad 1: (no net) -> Net-(C22-Pad1)
- C22 pad 2: (no net) -> GND
- C23 pad 1: (no net) -> /meter_2/I1N
- C23 pad 2: (no net) -> GND
- C24 pad 1: (no net) -> /meter_2/I2N
- C24 pad 2: (no net) -> GND
- C25 pad 1: (no net) -> /meter_2/I3N
- C25 pad 2: (no net) -> GND
- C26 pad 1: (no net) -> Net-(C26-Pad1)
- C26 pad 2: (no net) -> GND
- C27 pad 1: (no net) -> /meter_2/I1P
- C27 pad 2: (no net) -> GND
- C28 pad 1: (no net) -> /meter_2/I2P
- C28 pad 2: (no net) -> GND
- C29 pad 1: (no net) -> /meter_2/I3P
- C29 pad 2: (no net) -> GND
- C3 pad 1: (no net) -> +3V3
- C3 pad 2: (no net) -> GND
- C30 pad 1: (no net) -> Net-(C30-Pad1)
- C30 pad 2: (no net) -> GND
- C31 pad 1: (no net) -> Net-(C31-Pad1)
- C31 pad 2: (no net) -> GND
- C32 pad 1: (no net) -> Net-(C32-Pad1)
- C32 pad 2: (no net) -> GND
- C33 pad 1: (no net) -> Net-(C32-Pad1)
- C33 pad 2: (no net) -> GND
- C34 pad 1: (no net) -> +3V3
- C34 pad 2: (no net) -> GND
- C4 pad 1: (no net) -> Net-(C4-Pad1)
- C4 pad 2: (no net) -> GND
- C5 pad 1: (no net) -> /meter_1/I1N
- C5 pad 2: (no net) -> GND
- C6 pad 1: (no net) -> /meter_1/I2N
- C6 pad 2: (no net) -> GND
- C7 pad 1: (no net) -> /meter_1/I3N
- C7 pad 2: (no net) -> GND
- C8 pad 1: (no net) -> Net-(C8-Pad1)
- C8 pad 2: (no net) -> GND
- C9 pad 1: (no net) -> /meter_1/I1P
- C9 pad 2: (no net) -> GND
- IC1 pad 11: Net-(IC1-Pad11) -> Net-(C14-Pad1)
- IC1 pad 13: Net-(IC1-Pad13) -> Net-(C4-Pad1)
- IC1 pad 14: Net-(IC1-Pad14) -> Net-(C8-Pad1)
- IC1 pad 15: Net-(IC1-Pad15) -> Net-(C12-Pad1)
- IC1 pad 16: Net-(IC1-Pad16) -> Net-(C13-Pad1)
- IC1 pad 3: Net-(IC1-Pad3) -> /meter_1/I1P
- IC1 pad 4: Net-(IC1-Pad4) -> /meter_1/I1N
- IC1 pad 42: +3V3 -> /meter_1/1.8VDD
- IC1 pad 43: +3V3 -> /meter_1/1.8VDD
- IC1 pad 5: Net-(IC1-Pad5) -> /meter_1/I2P
- IC1 pad 6: Net-(IC1-Pad6) -> /meter_1/I2N
- IC1 pad 7: Net-(IC1-Pad7) -> /meter_1/I3P
- IC1 pad 8: Net-(IC1-Pad8) -> /meter_1/I3N
- IC2 pad 11: Net-(IC2-Pad11) -> Net-(C32-Pad1)
- IC2 pad 13: Net-(IC2-Pad13) -> Net-(C22-Pad1)
- IC2 pad 14: Net-(IC2-Pad14) -> Net-(C26-Pad1)
- IC2 pad 15: Net-(IC2-Pad15) -> Net-(C30-Pad1)
- IC2 pad 16: Net-(IC2-Pad16) -> Net-(C31-Pad1)
- IC2 pad 3: Net-(IC2-Pad3) -> /meter_2/I1P
- IC2 pad 4: Net-(IC2-Pad4) -> /meter_2/I1N
- IC2 pad 42: +3V3 -> /meter_2/1.8VDD
- IC2 pad 43: +3V3 -> /meter_2/1.8VDD
- IC2 pad 5: Net-(IC2-Pad5) -> /meter_2/I2P
- IC2 pad 6: Net-(IC2-Pad6) -> /meter_2/I2N
- IC2 pad 7: Net-(IC2-Pad7) -> /meter_2/I3P
- IC2 pad 8: Net-(IC2-Pad8) -> /meter_2/I3N
- J2 pad 11: /meter_1/IRQ1 -> /meter_1/SDO
- J2 pad 13: GND -> /meter_1/SCLK
- J2 pad 3: /meter_1/~CS -> +3V3
- J2 pad 4: /meter_2/~CS -> /meter_1/~CS
- J2 pad 5: /meter_1/SDI -> /meter_1/IRQ1
- J2 pad 6: /meter_2/IRQ1 -> /meter_2/~CS
- J2 pad 7: /meter_1/SDO -> /meter_2/IRQ1
- J2 pad 8: Net-(J2-Pad8) -> GND
- J2 pad 9: /meter_1/SCLK -> /meter_1/SDI
- R1 pad 1: (no net) -> +3V3
- R1 pad 2: (no net) -> /meter_1/~RESET
- R10 pad 1: (no net) -> Net-(CT2-1-Pad2)
- R10 pad 2: (no net) -> Net-(CT2-1-Pad1)
- R11 pad 1: (no net) -> Net-(CT3-1-Pad2)
- R11 pad 2: (no net) -> Net-(CT3-1-Pad1)
- R12 pad 1: (no net) -> Net-(CT1-1-Pad1)
- R12 pad 2: (no net) -> /meter_1/I1P
- R13 pad 1: (no net) -> Net-(CT1-1-Pad2)
- R13 pad 2: (no net) -> /meter_1/I1N
- R14 pad 1: (no net) -> Net-(CT2-1-Pad1)
- R14 pad 2: (no net) -> /meter_1/I2P
- R15 pad 1: (no net) -> Net-(CT2-1-Pad2)
- R15 pad 2: (no net) -> /meter_1/I2N
- R16 pad 1: (no net) -> Net-(CT3-1-Pad1)
- R16 pad 2: (no net) -> /meter_1/I3P
- R17 pad 1: (no net) -> Net-(CT3-1-Pad2)
- R17 pad 2: (no net) -> /meter_1/I3N
- R18 pad 1: (no net) -> GND
- R18 pad 2: (no net) -> Net-(C12-Pad1)
- R19 pad 1: (no net) -> GND
- R19 pad 2: (no net) -> Net-(C13-Pad1)
- R2 pad 1: (no net) -> Net-(CF1-PadA)
- R2 pad 2: (no net) -> +3V3
- R20 pad 1: (no net) -> /meter_1/SDO
- R20 pad 2: (no net) -> Net-(IC1-Pad39)
- R21 pad 1: (no net) -> +3V3
- R21 pad 2: (no net) -> /meter_1/~CS
- R22 pad 1: (no net) -> Net-(IC1-Pad25)
- R22 pad 2: (no net) -> Net-(CF2-PadA)
- R23 pad 1: (no net) -> Net-(IC1-Pad29)
- R23 pad 2: (no net) -> Net-(CF3-PadA)
- R24 pad 1: (no net) -> /meter_1/IRQ1
- R24 pad 2: (no net) -> Net-(CF4-PadA)
- R25 pad 1: (no net) -> Net-(C22-Pad1)
- R25 pad 2: (no net) -> /meter_1/V1P
- R26 pad 1: (no net) -> Net-(C26-Pad1)
- R26 pad 2: (no net) -> /meter_1/V1N
- R27 pad 1: (no net) -> Net-(C30-Pad1)
- R27 pad 2: (no net) -> /meter_1/V2P
- R28 pad 1: (no net) -> Net-(C31-Pad1)
- R28 pad 2: (no net) -> /meter_1/V2N
- R29 pad 1: (no net) -> GND
- R29 pad 2: (no net) -> Net-(C22-Pad1)
- R3 pad 1: (no net) -> Net-(C4-Pad1)
- R3 pad 2: (no net) -> /meter_1/V1P
- R30 pad 1: (no net) -> GND
- R30 pad 2: (no net) -> Net-(C26-Pad1)
- R31 pad 1: (no net) -> Net-(CT1-2-Pad2)
- R31 pad 2: (no net) -> Net-(CT1-2-Pad1)
- R32 pad 1: (no net) -> Net-(CT2-2-Pad2)
- R32 pad 2: (no net) -> Net-(CT2-2-Pad1)
- R33 pad 1: (no net) -> Net-(CT3-2-Pad2)
- R33 pad 2: (no net) -> Net-(CT3-2-Pad1)
- R34 pad 1: (no net) -> Net-(CT1-2-Pad1)
- R34 pad 2: (no net) -> /meter_2/I1P
- R35 pad 1: (no net) -> Net-(CT1-2-Pad2)
- R35 pad 2: (no net) -> /meter_2/I1N
- R36 pad 1: (no net) -> Net-(CT2-2-Pad1)
- R36 pad 2: (no net) -> /meter_2/I2P
- R37 pad 1: (no net) -> Net-(CT2-2-Pad2)
- R37 pad 2: (no net) -> /meter_2/I2N
- R38 pad 1: (no net) -> Net-(CT3-2-Pad1)
- R38 pad 2: (no net) -> /meter_2/I3P
- R39 pad 1: (no net) -> Net-(CT3-2-Pad2)
- R39 pad 2: (no net) -> /meter_2/I3N
- R4 pad 1: (no net) -> Net-(C8-Pad1)
- R4 pad 2: (no net) -> /meter_1/V1N
- R40 pad 1: (no net) -> GND
- R40 pad 2: (no net) -> Net-(C30-Pad1)
- R41 pad 1: (no net) -> GND
- R41 pad 2: (no net) -> Net-(C31-Pad1)
- R42 pad 1: (no net) -> /meter_1/SDO
- R42 pad 2: (no net) -> Net-(IC2-Pad39)
- R43 pad 1: (no net) -> +3V3
- R43 pad 2: (no net) -> /meter_2/~CS
- R44 pad 1: (no net) -> Net-(IC2-Pad25)
- R44 pad 2: (no net) -> Net-(CF5-PadA)
- R45 pad 1: (no net) -> Net-(IC2-Pad29)
- R45 pad 2: (no net) -> Net-(CF6-PadA)
- R46 pad 1: (no net) -> /meter_2/IRQ1
- R46 pad 2: (no net) -> Net-(CF7-PadA)
- R5 pad 1: (no net) -> Net-(C12-Pad1)
- R5 pad 2: (no net) -> /meter_1/V2P
- R6 pad 1: (no net) -> Net-(C13-Pad1)
- R6 pad 2: (no net) -> /meter_1/V2N
- R7 pad 1: (no net) -> GND
- R7 pad 2: (no net) -> Net-(C4-Pad1)
- R8 pad 1: (no net) -> GND
- R8 pad 2: (no net) -> Net-(C8-Pad1)
- R9 pad 1: (no net) -> Net-(CT1-1-Pad2)
- R9 pad 2: (no net) -> Net-(CT1-1-Pad1)
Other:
- board outline added: 60 x 100 mm

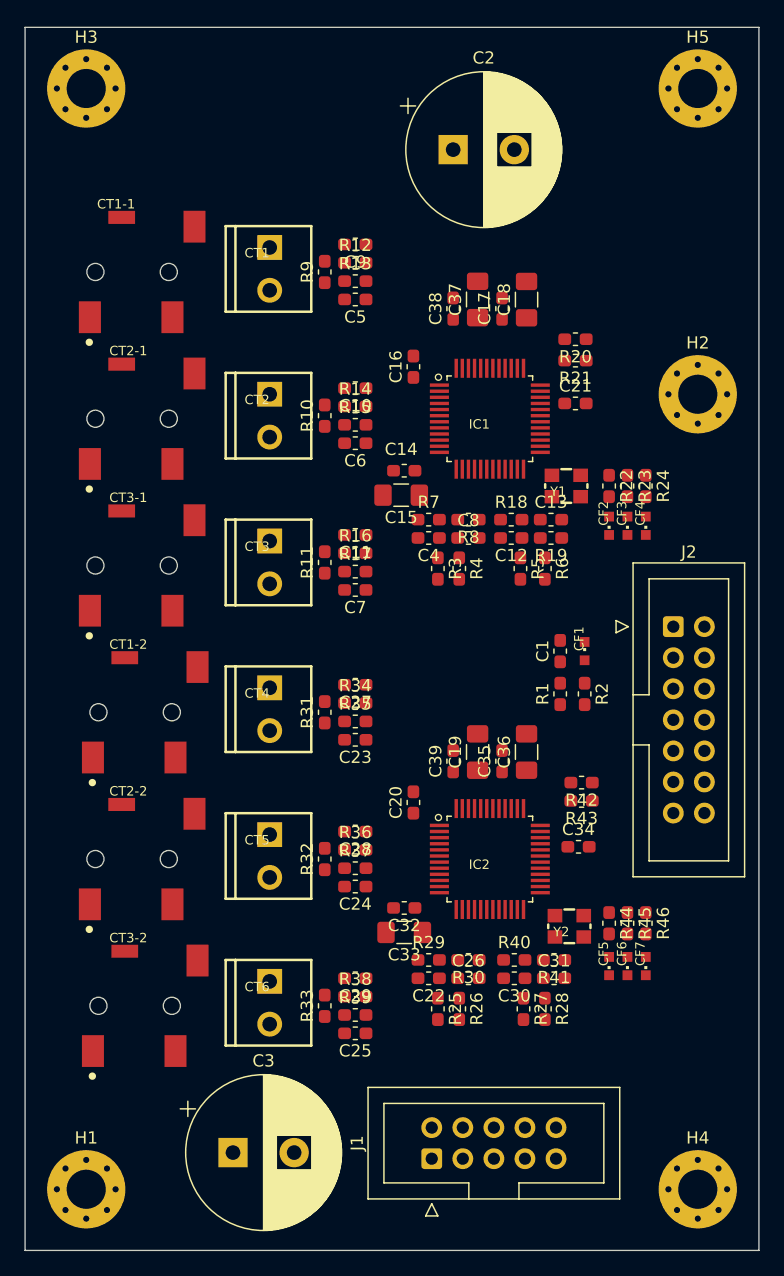
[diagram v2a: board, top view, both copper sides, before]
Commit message: Minor footprint cleanup.
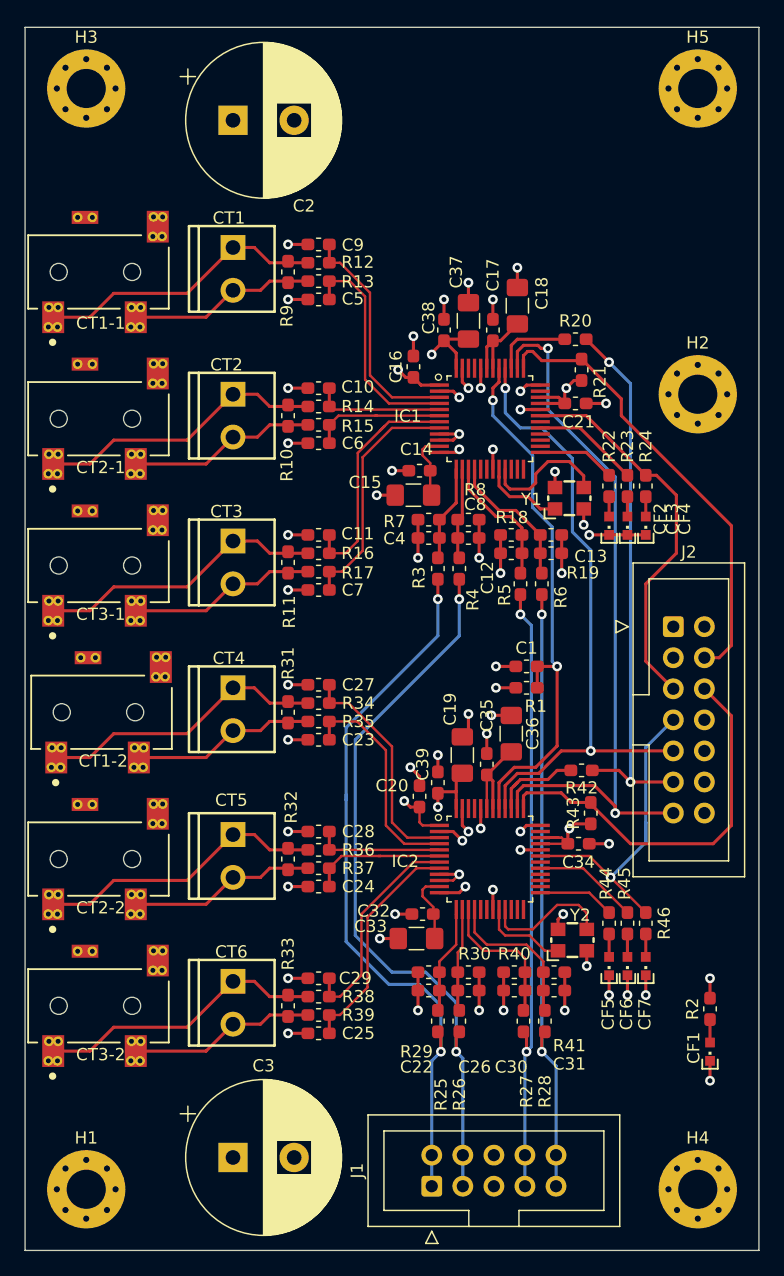
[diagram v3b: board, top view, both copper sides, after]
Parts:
- moved CF1 34.3 mm to (91.0, 118.8), turned to 180 degrees
- moved R2 27.7 mm to (91.0, 115.2), turned to 90 degrees
- moved C2 18.2 mm to (52.0, 42.6)
- moved CT3-2 3.25 mm to (41.0, 115.0)
- moved C1 3.02 mm to (76.0, 87.2), turned to 180 degrees
- moved C10 3.00 mm to (59.0, 64.5)
- moved C11 3.00 mm to (59.0, 76.5)
- moved C23 3.00 mm to (59.0, 93.2)
- moved C24 3.00 mm to (59.0, 105.2)
- moved C25 3.00 mm to (59.0, 117.2)
- moved C27 3.00 mm to (59.0, 88.8)
- moved C28 3.00 mm to (59.0, 100.8)
- moved C29 3.00 mm to (59.0, 112.8)
- moved C5 3.00 mm to (59.0, 57.2)
- moved C6 3.00 mm to (59.0, 69.0)
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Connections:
- J1 pad 2: /meter_1/V1N -> /meter_1/V1P
- J1 pad 3: /meter_1/V1P -> /meter_1/V1N
- J1 pad 8: /meter_1/V2N -> /meter_1/V2P
- J1 pad 9: /meter_1/V2P -> /meter_1/V2N
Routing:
- net GND: track 0.00 -> 120.7 mm, vias 0 -> 62
- net /meter_1/V1N: track 0.00 -> 60.1 mm, vias 0 -> 2
- net /meter_1/SCLK: track 0.00 -> 60.1 mm, vias 0 -> 2
- net /meter_1/V1P: track 0.00 -> 59.8 mm, vias 0 -> 2
- net /meter_1/SDI: track 0.00 -> 52.1 mm, vias 0 -> 2
- net /meter_1/V2P: track 0.00 -> 50.7 mm, vias 0 -> 2
- net /meter_1/V2N: track 0.00 -> 50.6 mm, vias 0 -> 2
- net /meter_1/SDO: track 0.00 -> 44.8 mm, vias 0 -> 2
- net /meter_1/~RESET: track 0.00 -> 44.7 mm, vias 0 -> 2
- net +3V3: track 0.00 -> 40.6 mm, vias 0 -> 8
- net /meter_1/~CS: track 0.00 -> 37.4 mm
- net /meter_2/~CS: track 0.00 -> 32.6 mm
- net /meter_1/IRQ1: track 0.00 -> 31.6 mm
- net /meter_2/IRQ1: track 0.00 -> 27.3 mm, vias 0 -> 1
- net Net-(CT3-2-Pad1): track 0.00 -> 23.7 mm
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- added copper zone on In2.Cu, net +3V3
- added copper zone on In1.Cu, net GND
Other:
- copper layers 2 -> 4
- net class 2 added: clearance 0.2, trace_width 0.381, via_dia 0.8, via_drill 0.4
- net class 3 added: clearance 0.2, trace_width 0.508, via_dia 0.8, via_drill 0.4
- net class Default: trace_width 0.25 -> 0.254
